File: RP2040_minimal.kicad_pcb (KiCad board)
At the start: 2 copper layers, 52 x 51 mm, 34 parts, among them J1 USB_B_Micro, J2 Conn_01x02, J3 Conn_02x18_Odd_Even, J4 Conn_02x18_Odd_Even, U1 NCP1117-3.3_SOT223, U2 W25Q128JVS, U3 RP2040, Y1 ABLS-12.000MHZ-B4-T

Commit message: .pcb and .sch saved as version kicad 6.0
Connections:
- net /~USB_BOOT renamed /~{USB_BOOT}
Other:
- net class Default removed
- net class USB_DIFF_90 removed

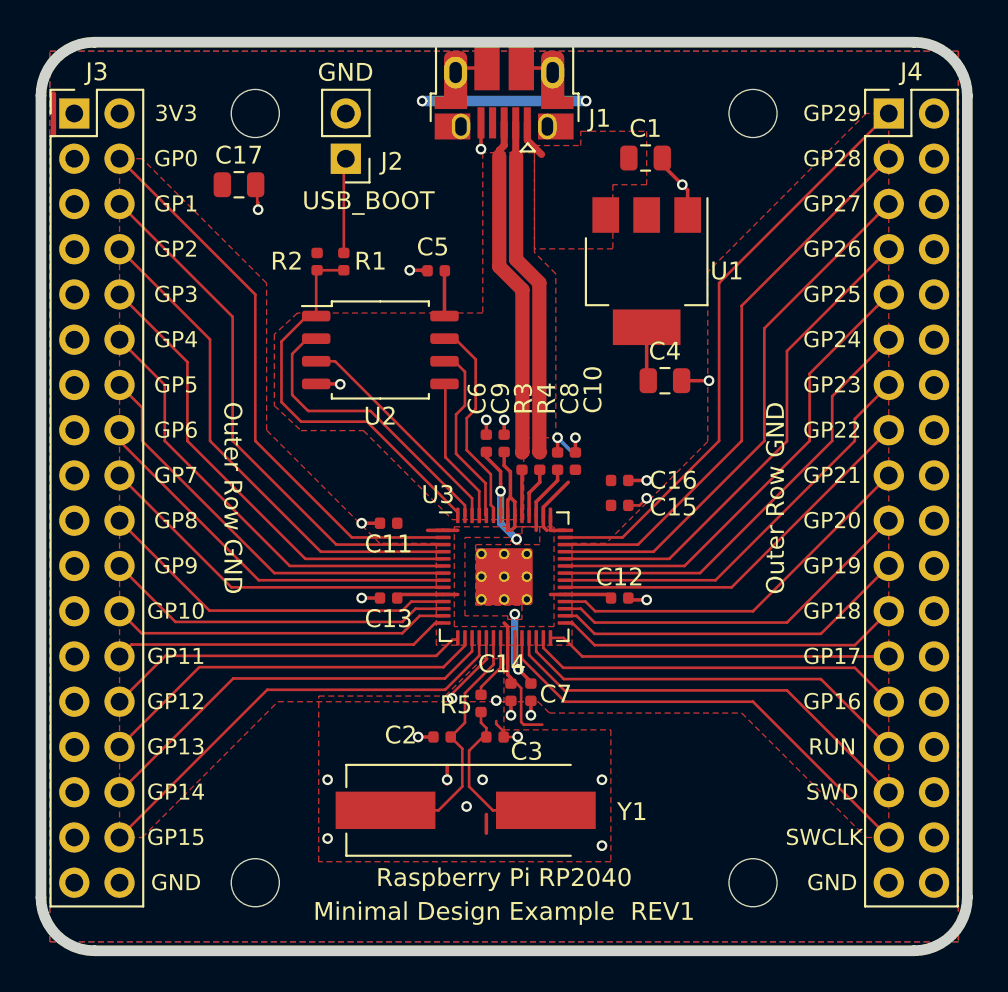
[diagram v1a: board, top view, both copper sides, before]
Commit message: Prettied up the component and route placement.
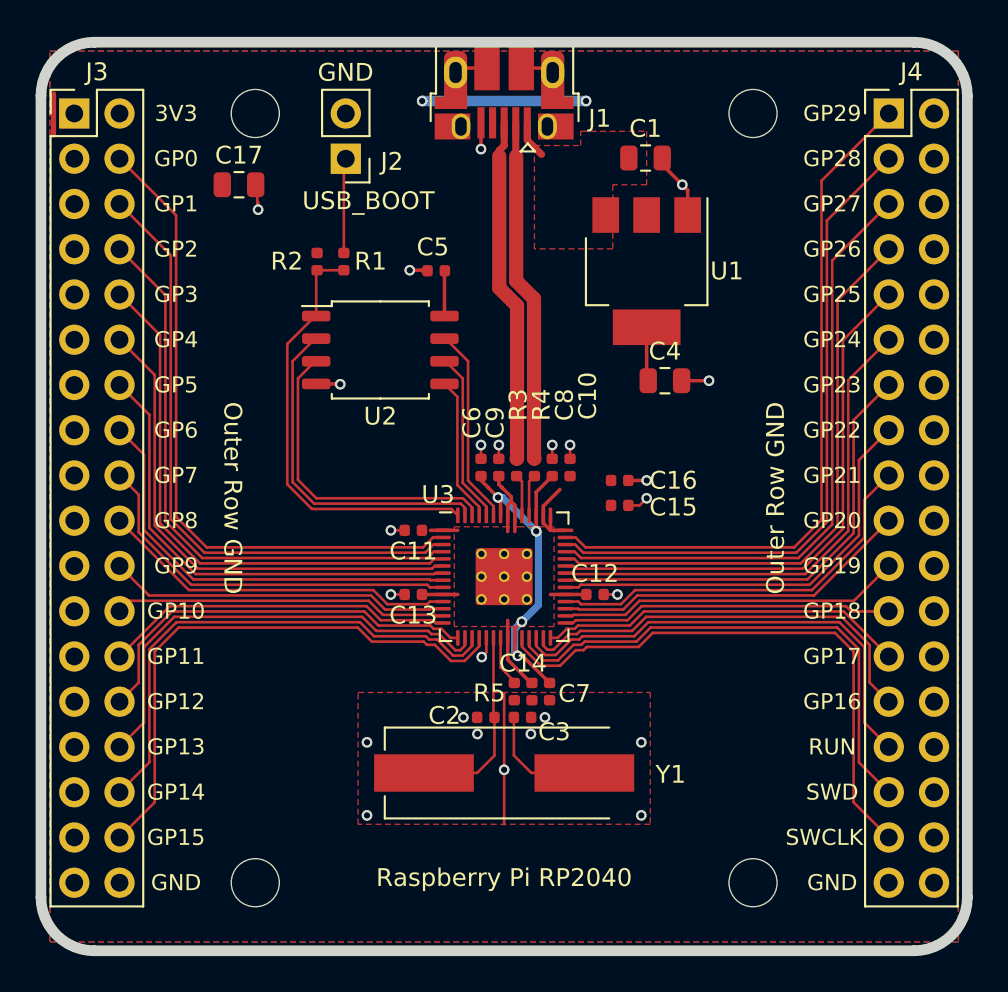
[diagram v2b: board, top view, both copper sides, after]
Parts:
- moved Y1 3.01 mm to (100.0, 111.0)
- moved C2 2.69 mm to (99.0, 107.9)
- moved R5 1.98 mm to (100.6, 106.5)
- moved C3 1.90 mm to (101.0, 107.9)
- moved C11 1.44 mm to (94.9, 97.4)
- moved C12 1.40 mm to (105.1, 101.0)
- moved C13 1.40 mm to (94.9, 101.0)
- moved C6 1.39 mm to (98.7, 93.9)
- moved C9 1.39 mm to (99.7, 93.9)
- moved C14 1.18 mm to (101.6, 106.5)
- moved C7 1.05 mm to (102.5, 106.5)
- moved C10 0.46 mm to (103.7, 93.9)
- moved C8 0.46 mm to (102.7, 93.9)
- moved R3 0.46 mm to (100.7, 93.9)
- moved R4 0.46 mm to (101.7, 93.9)
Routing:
- net +3V3: track 45.2 -> 36.5 mm
- net /GPIO29_ADC3: track 33.2 -> 39.6 mm
- net /GPIO15: track 25.4 -> 31.6 mm
- net /SWCLK: track 25.9 -> 32.0 mm
- net /GPIO28_ADC2: track 31.6 -> 37.4 mm
- net /GPIO0: track 31.8 -> 37.3 mm
- net /GPIO27_ADC1: track 29.9 -> 35.2 mm
- net /GPIO14: track 23.8 -> 28.9 mm
- net /QSPI_SD2: track 12.9 -> 18.0 mm
- net /GPIO1: track 30.2 -> 35.1 mm
- net /SWD: track 24.3 -> 29.3 mm
- net /GPIO26_ADC0: track 28.3 -> 33.0 mm
- net GND: track 34.8 -> 30.4 mm, vias 28 -> 25
- net /GPIO2: track 28.5 -> 32.9 mm
- net /GPIO25: track 26.7 -> 30.8 mm
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- removed copper zone on F.Cu, net +1V1
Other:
- board text removed: "Minimal Design Example REV1"

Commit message: Moved processor, flash, crystal and associated passives towards bottom of board.
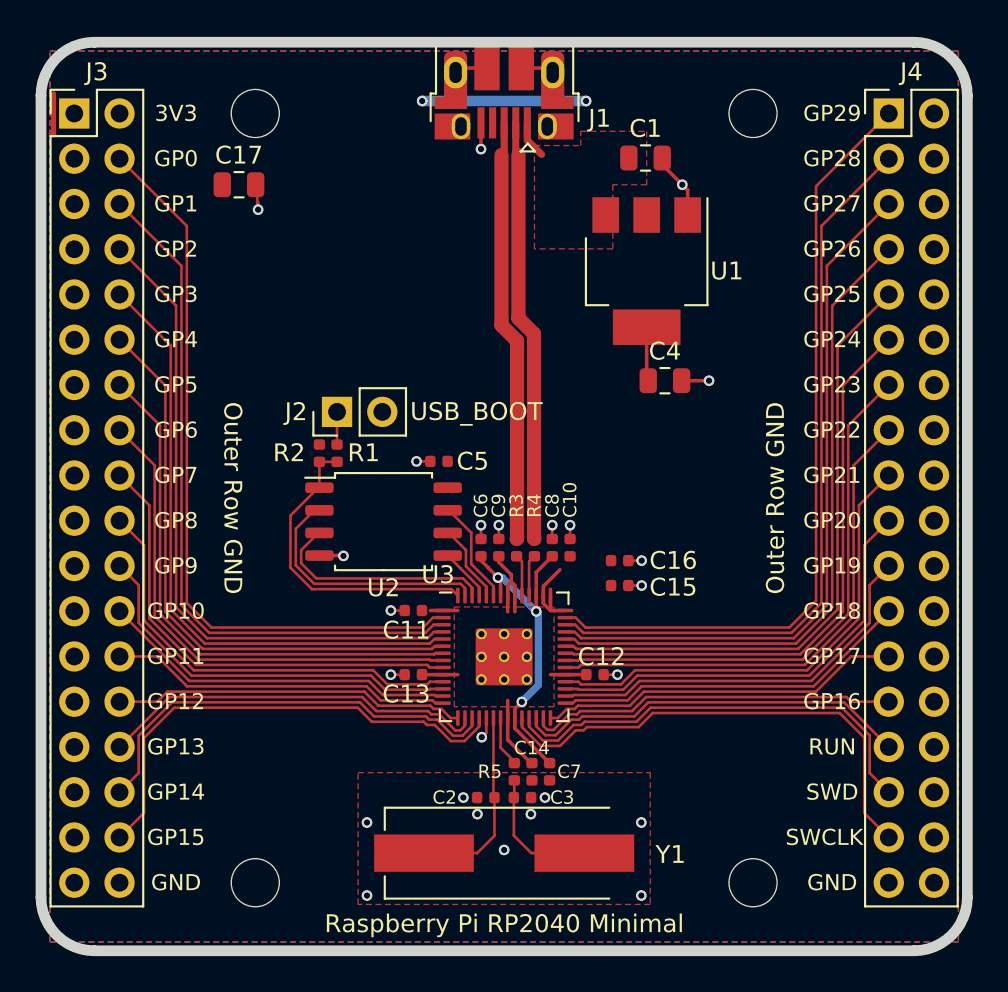
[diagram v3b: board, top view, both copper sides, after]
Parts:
- moved J2 14.2 mm to (90.6, 90.8), turned to 90 degrees
- moved R1 10.8 mm to (90.6, 93.1)
- moved R2 10.8 mm to (89.6, 93.1)
- moved C5 10.7 mm to (96.3, 93.5)
- moved U2 9.64 mm to (93.2, 96.9)
- moved C10 4.50 mm to (103.7, 98.4)
- moved C11 4.50 mm to (94.9, 101.9)
- moved C12 4.50 mm to (105.1, 105.5)
- moved C13 4.50 mm to (94.9, 105.5)
- moved C14 4.50 mm to (101.6, 111.0)
- moved C15 4.50 mm to (106.5, 100.5)
- moved C16 4.50 mm to (106.5, 99.1)
- moved C2 4.50 mm to (99.0, 112.4)
- moved C3 4.50 mm to (101.0, 112.4)
- moved C6 4.50 mm to (98.7, 98.4)
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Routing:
- net GND: track 30.4 -> 22.1 mm
- net /QSPI_SS: track 24.6 -> 17.7 mm
- net /QSPI_SD2: track 18.0 -> 12.8 mm
- net /QSPI_SD0: track 8.20 -> 2.99 mm
- net /QSPI_SD3: track 11.1 -> 5.89 mm
- net /QSPI_SCLK: track 9.67 -> 4.46 mm
- net /QSPI_SD1: track 19.3 -> 14.3 mm
- net /USB_D-: track 19.3 -> 23.8 mm
- net /USB_D+: track 19.4 -> 23.8 mm
- net /GPIO15: track 31.6 -> 27.3 mm
- net /GPIO14: track 28.9 -> 24.6 mm
- net /GPIO28_ADC2: track 37.4 -> 41.8 mm
- net /GPIO3: track 30.7 -> 35.1 mm
- net /GPIO0: track 37.3 -> 41.7 mm
- net /SWCLK: track 32.0 -> 27.7 mm
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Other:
- board text added: "Raspberry Pi RP2040 Minimal"
- board text removed: "Raspberry Pi RP2040"

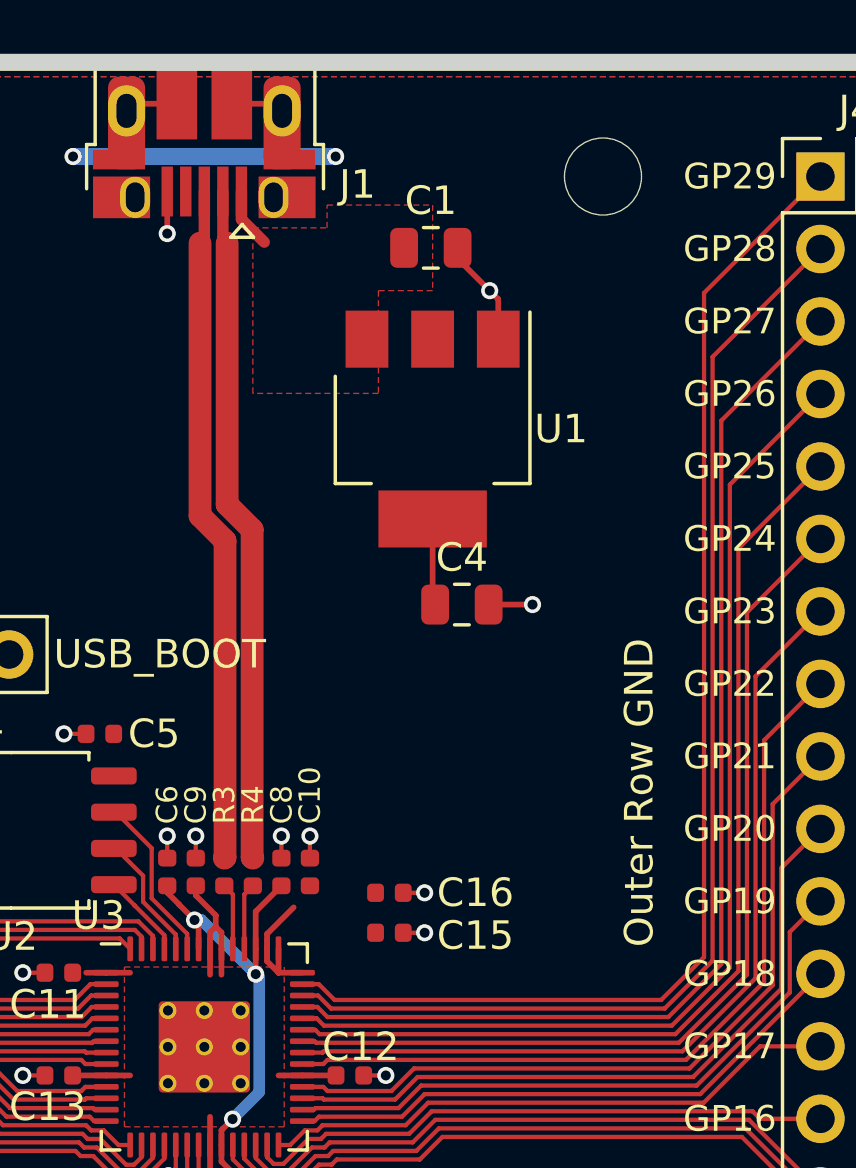
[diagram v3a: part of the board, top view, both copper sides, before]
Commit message: Deleted flood fill for VBUS, tightened up passives for 3.3v regulator. Moved 3.3v regulator towards processor.
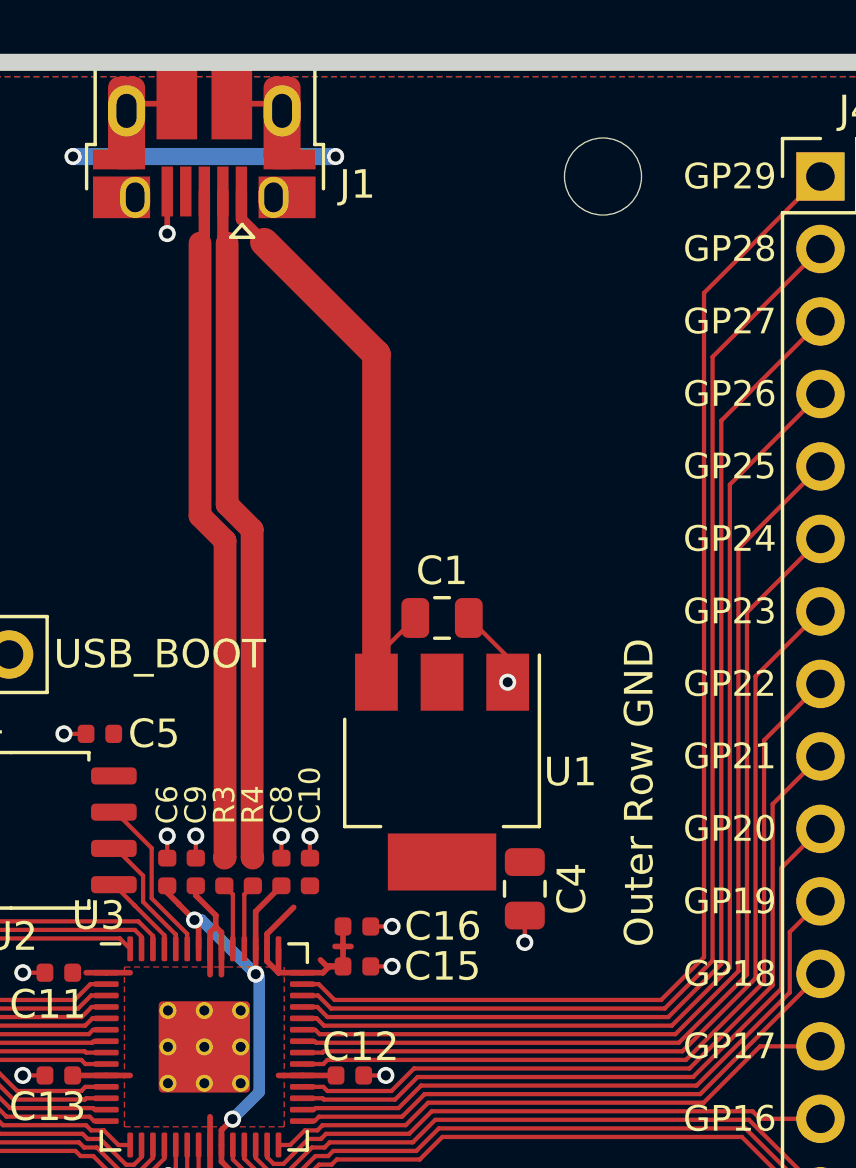
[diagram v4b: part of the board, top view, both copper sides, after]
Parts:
- moved C1 13.0 mm to (108.3, 89.5)
- moved U1 12.0 mm to (108.3, 94.9)
- moved C4 10.2 mm to (111.2, 99.0), turned to -90 degrees
- moved C15 1.64 mm to (105.3, 101.7)
- moved C16 1.64 mm to (105.3, 100.3)
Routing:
- net VBUS: track 2.11 -> 22.0 mm
- net GND: track 22.1 -> 20.6 mm
- net +3V3: track 33.9 -> 35.3 mm
- removed copper zone on F.Cu, net VBUS

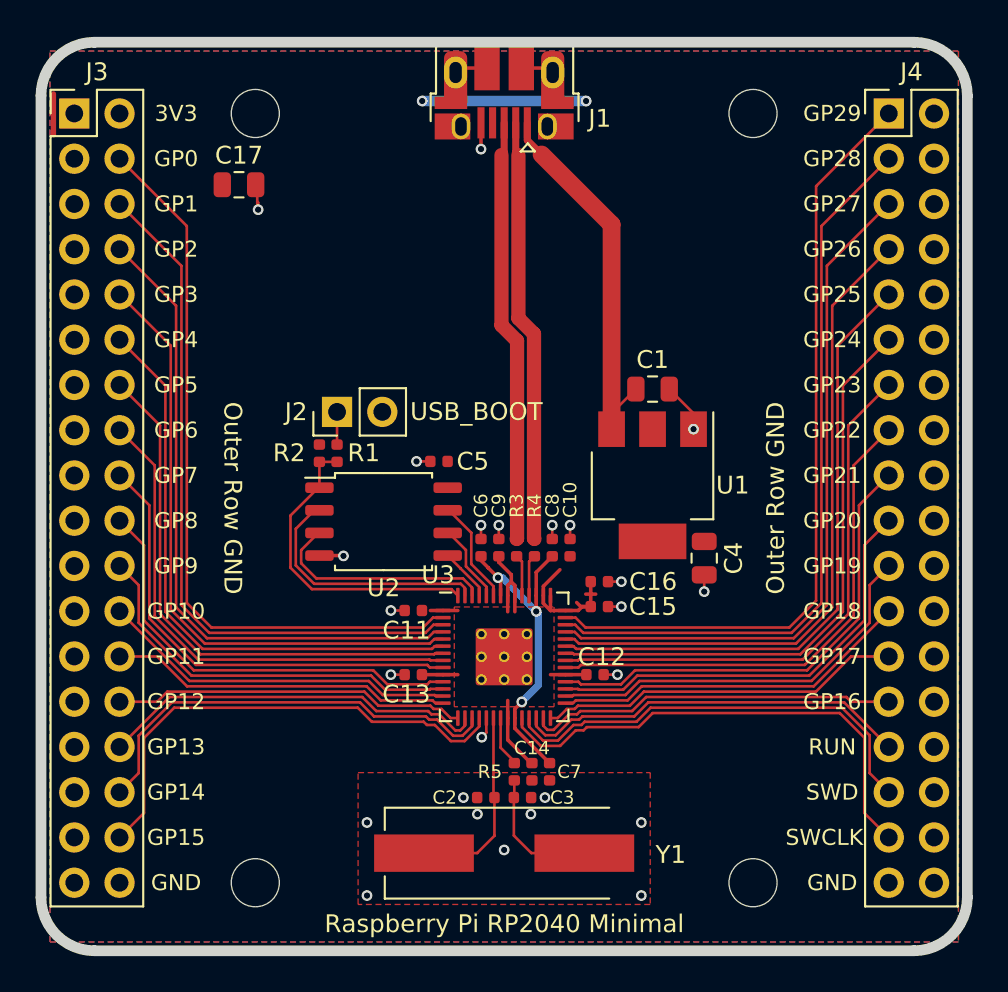
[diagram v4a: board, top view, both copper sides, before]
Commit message: Updated sheet information, renumbered annotation for capacitors.
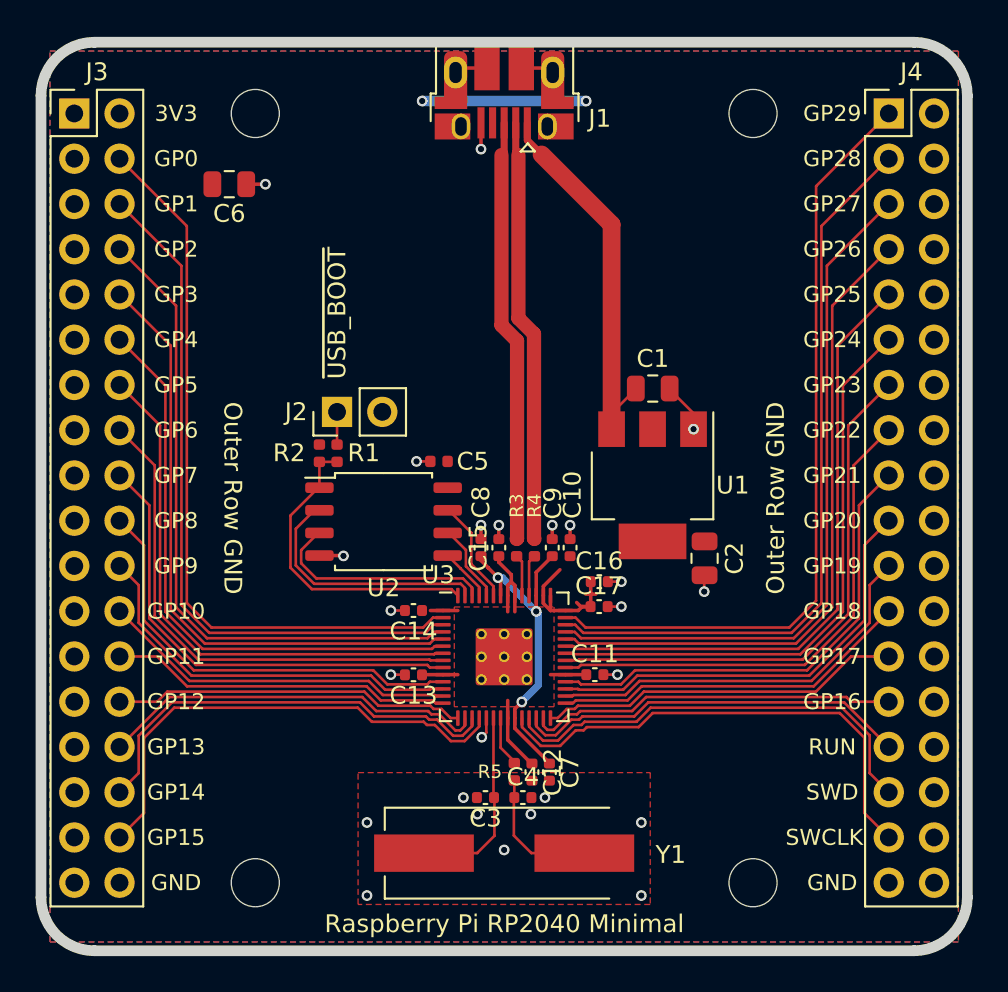
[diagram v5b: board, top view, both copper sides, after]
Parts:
- C17: value 10u -> 100n; footprint Capacitor_SMD:C_0805_2012Metric -> Capacitor_SMD:C_0402_1005Metric
- C2: value 27p -> 10u; footprint Capacitor_SMD:C_0402_1005Metric -> Capacitor_SMD:C_0805_2012Metric
- C4: value 10u -> 27p; footprint Capacitor_SMD:C_0805_2012Metric -> Capacitor_SMD:C_0402_1005Metric
- C6: value 100n -> 10u; footprint Capacitor_SMD:C_0402_1005Metric -> Capacitor_SMD:C_0805_2012Metric
- C8: value 1u -> 100n
- C9: value 100n -> 1u
- moved C17 31.1 mm to (105.3, 101.7)
- moved C6 24.8 mm to (84.6, 78.0), turned to 0 degrees
- moved C2 18.2 mm to (111.2, 99.0), turned to -90 degrees
- moved C4 16.9 mm to (101.0, 112.4), turned to 0 degrees
- moved C14 11.2 mm to (94.9, 101.9), turned to 180 degrees
- moved C11 10.8 mm to (105.1, 105.5), turned to 0 degrees
- moved C15 6.54 mm to (99.7, 98.4), turned to 90 degrees
- moved C12 6.52 mm to (101.6, 111.0), turned to -90 degrees
- moved C8 4.00 mm to (98.7, 98.4)
- moved C9 3.00 mm to (102.7, 98.4)
- moved C3 2.08 mm to (99.0, 112.4), turned to 180 degrees
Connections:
- C2 pad 1: /XIN -> +3V3
- C3 pad 1: Net-(C3-Pad1) -> /XIN
- C4 pad 1: +3V3 -> Net-(C4-Pad1)
- C6 pad 1: +1V1 -> +3V3
- C9 pad 1: +3V3 -> +1V1
- J1 pad 4: Net-(J1-Pad4) -> unconnected-(J1-Pad4)
- R5 pad 2: Net-(C3-Pad1) -> Net-(C4-Pad1)
- Y1 pad 2: Net-(C3-Pad1) -> Net-(C4-Pad1)
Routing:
- net Net-(C4-Pad1): track 0.00 -> 7.52 mm
- net Net-(C3-Pad1): track 7.52 -> 0.00 mm
- net +3V3: track 35.3 -> 33.0 mm
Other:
- board text added: "~{USB_BOOT}"
- board text removed: "USB_BOOT"
